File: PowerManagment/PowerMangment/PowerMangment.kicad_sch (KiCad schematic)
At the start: 14 parts, among them J1 Barrel_Jack_Switch, J2 USB_B_Micro, Q1 IRF4905, U1 TP4056(Module), U2 MT3608(Module), U3 MCP6024

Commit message: Hungry Hamster: Measure metrics obtained
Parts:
- R2: value 1.2K -> 12K
- R3: value 2.2K -> 22K
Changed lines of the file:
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@@
       (effects (font (size 1.27 1.27)) (justify left))
     )
-    (property "Value" "1.2K" (at 152.4 104.775 0)
+    (property "Value" "12K" (at 152.4 104.775 0)
       (effects (font (size 1.27 1.27)) (justify left))
     )
@@
       (effects (font (size 1.27 1.27)) (justify left))
     )
-    (property "Value" "2.2K" (at 152.4 118.11 0)
+    (property "Value" "22K" (at 152.4 118.11 0)
       (effects (font (size 1.27 1.27)) (justify left))
     )

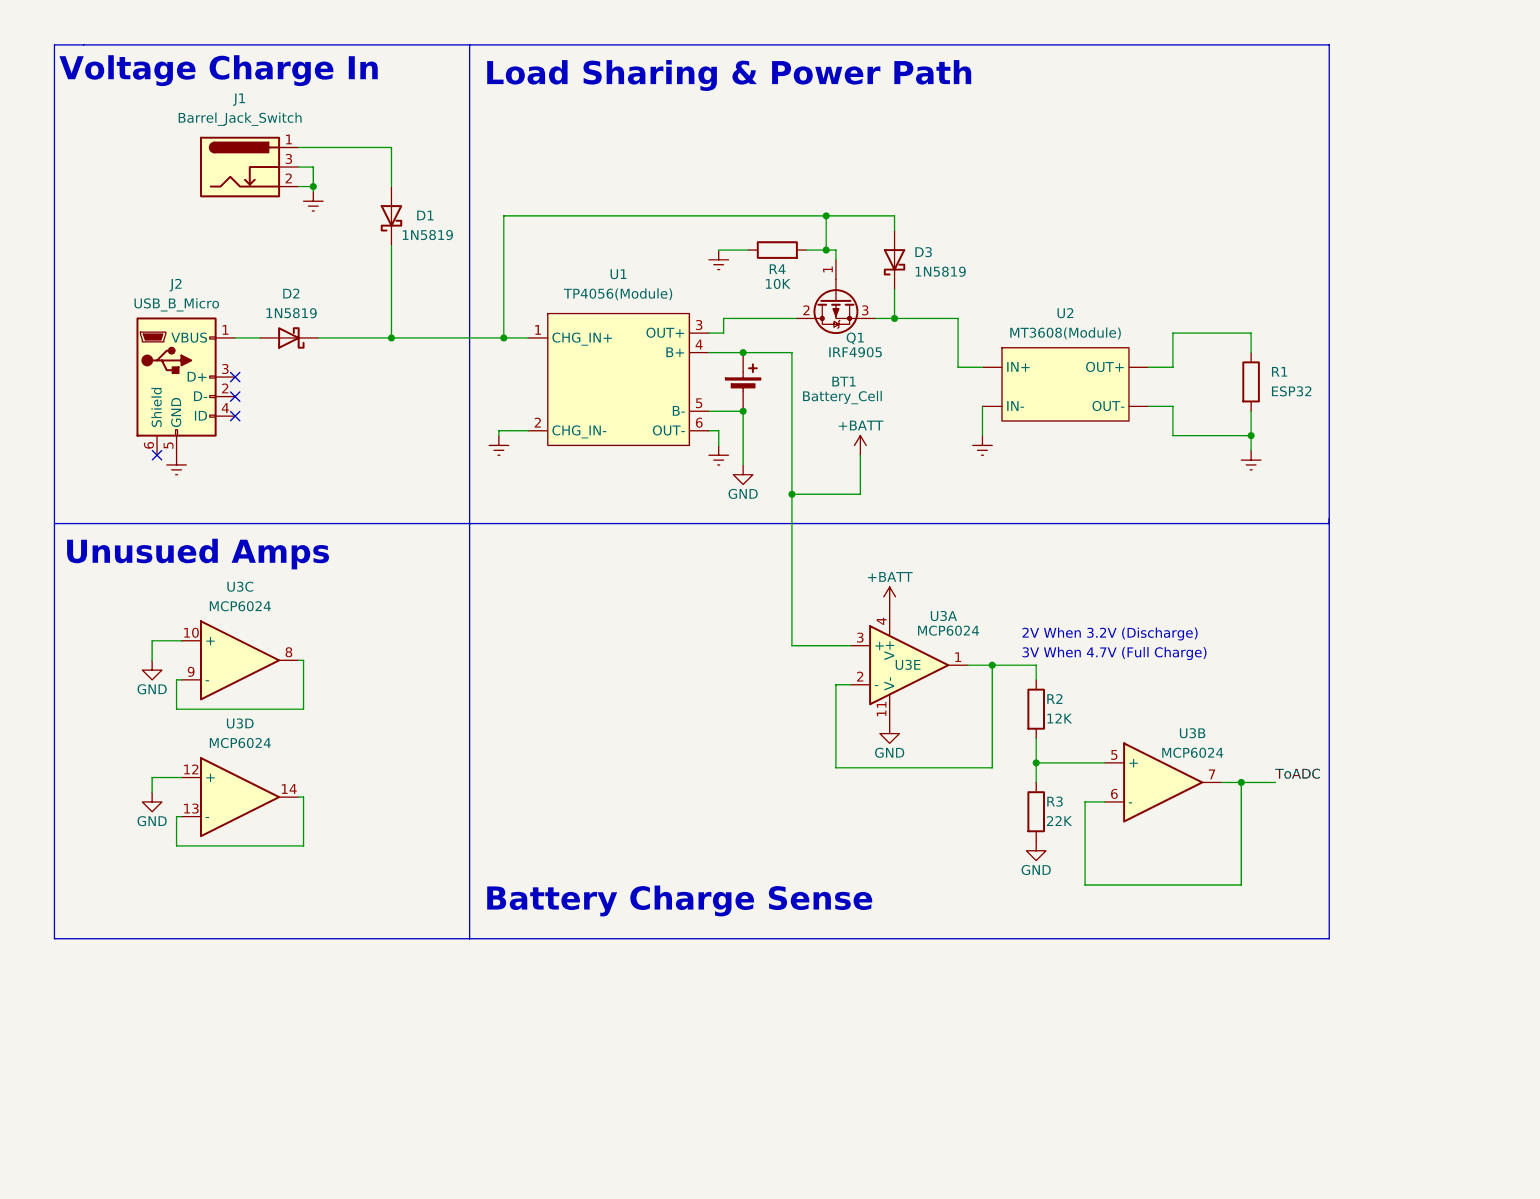
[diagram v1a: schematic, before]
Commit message: Power Circuit Adjust due to bypass short citcuit protection
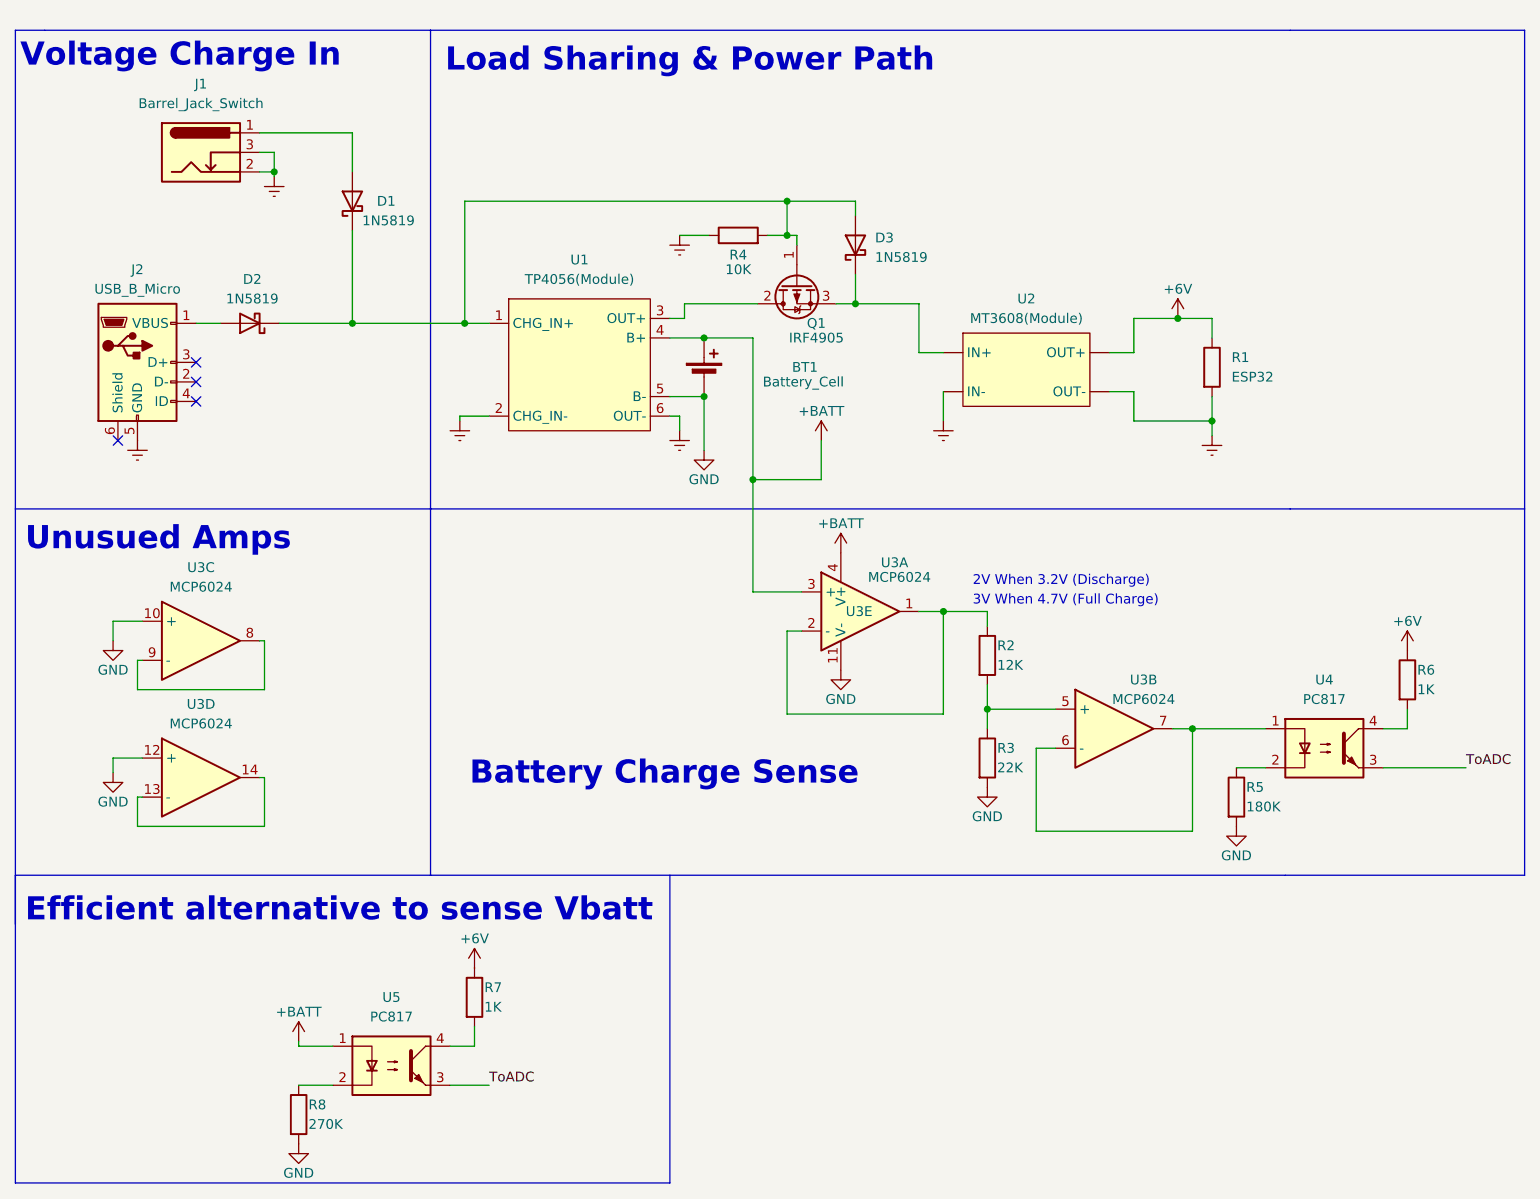
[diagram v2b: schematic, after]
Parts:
- added R5: 180K, symbol Device:R
- added R6, R7: 1K, symbol Device:R
- added R8: 270K, symbol Device:R
- added U4, U5: PC817, Package_DIP:DIP-4_W7.62mm, symbol Isolator:PC817
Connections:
- net +BATT: now also U5.1
- net GND: now also R5.2, R8.2
- net ToADC: now also U4.3, U5.3; no longer U3.6 (-), U3.7
- net +6V: now reaches R1.1, U2. (OUT-)
- net +6V: now also R6.1, R7.1
- new net: R8.1, U5.2
- new net: R7.2, U5.4
- new net: R5.1, U4.2
- new net: U3.6 (-), U3.7, U4.1
- new net: R6.2, U4.4
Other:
- note added: "Efficient alternative to sense Vbatt"
- moved on the sheet: BT1, D1, D2, D3, J1, J2, Q1, R1, R2, R3, R4, U1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

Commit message: Power system changed to AA batteries
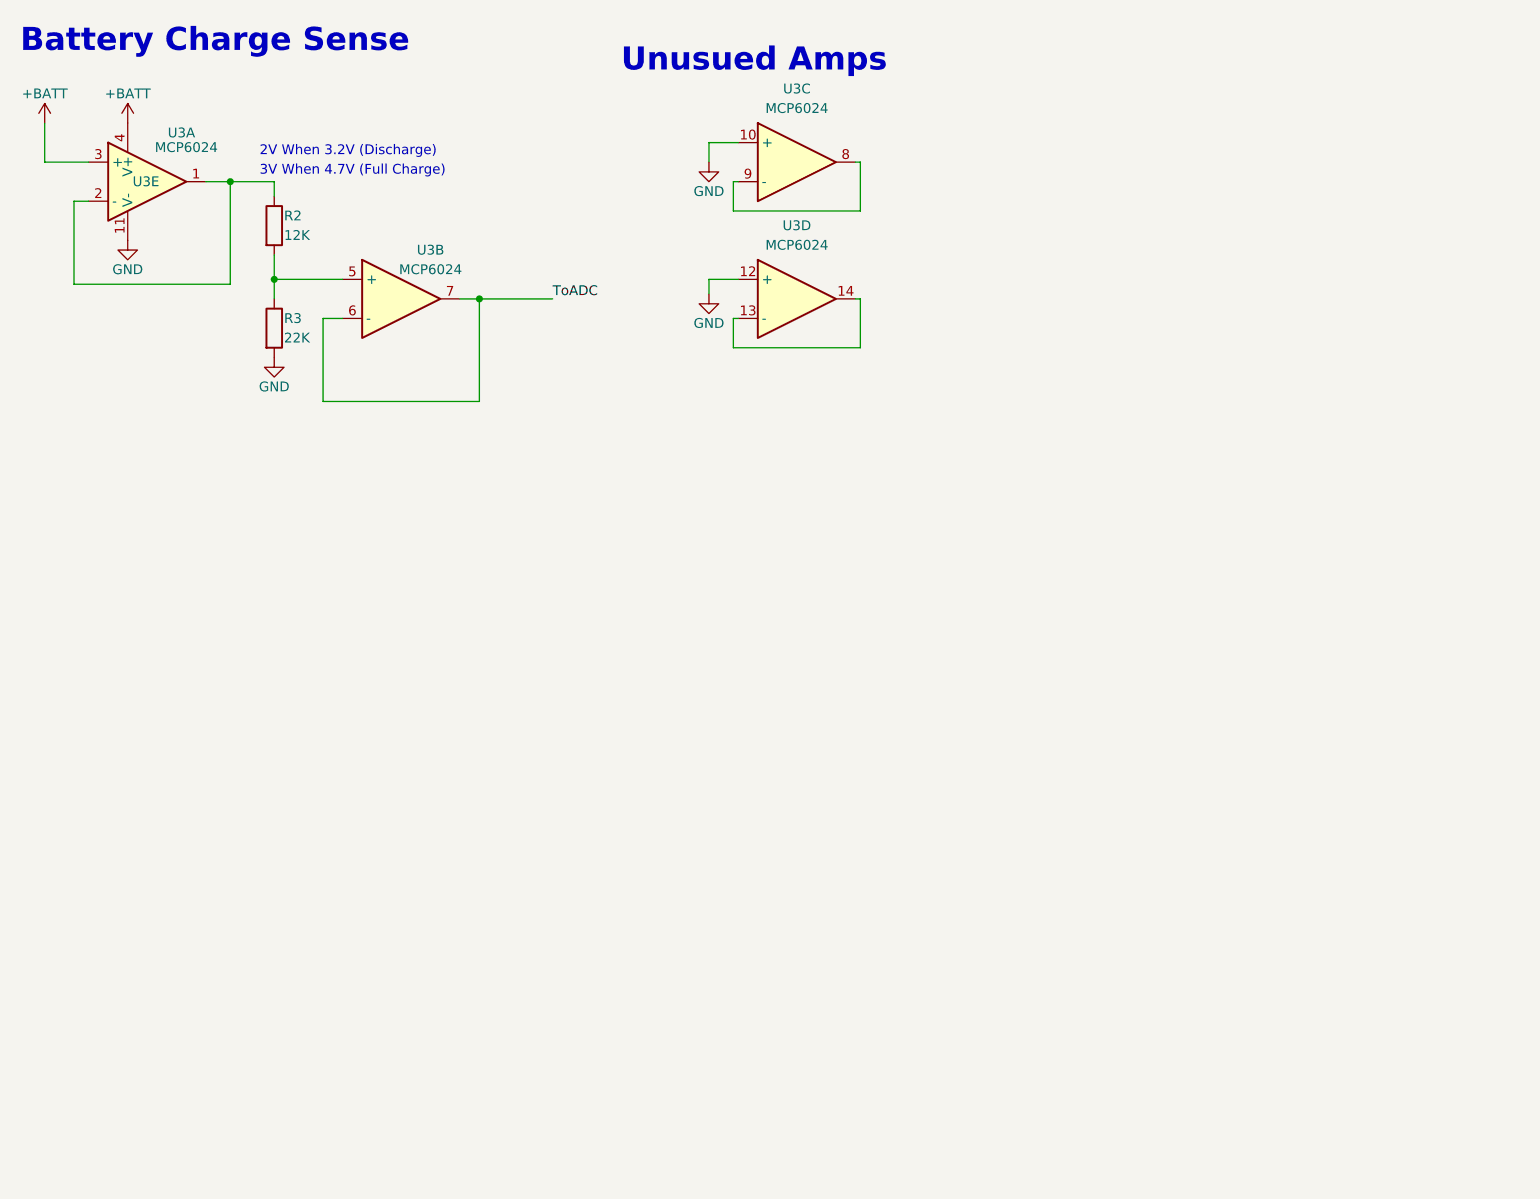
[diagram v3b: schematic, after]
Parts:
- removed BT1: Battery_Cell, symbol Device:Battery_Cell
- removed D1, D2, D3: 1N5819, Diode_THT:D_DO-41_SOD81_P10.16mm_Horizontal, symbol Diode:1N5819
- removed J1: Barrel_Jack_Switch, symbol Connector:Barrel_Jack_Switch
- removed J2: USB_B_Micro, symbol Connector:USB_B_Micro
- removed Q1: IRF4905, Package_TO_SOT_THT:TO-220-3_Vertical, symbol Transistor_FET:IRF4905
- removed R1: ESP32, symbol Device:R
- removed R4: 10K, symbol Device:R
- removed R5: 180K, symbol Device:R
- removed R6, R7: 1K, symbol Device:R
- removed R8: 270K, symbol Device:R
- removed U1: TP4056(Module), symbol Modulos:TP4056(Module)
- removed U2: MT3608(Module), symbol Modulos:MT3608(Module)
- removed U4, U5: PC817, Package_DIP:DIP-4_W7.62mm, symbol Isolator:PC817
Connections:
- net ToADC: now also U3.6 (-), U3.7
- no-connect marks 4 -> 0
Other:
- note removed: "Efficient alternative to sense Vbatt"
- note removed: "Load Sharing & Power Path"
- note removed: "Voltage Charge In"
- moved on the sheet: R2, R3, U3A, U3B, U3C, U3D, U3E
